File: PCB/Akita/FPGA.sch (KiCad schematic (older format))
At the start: 4 parts

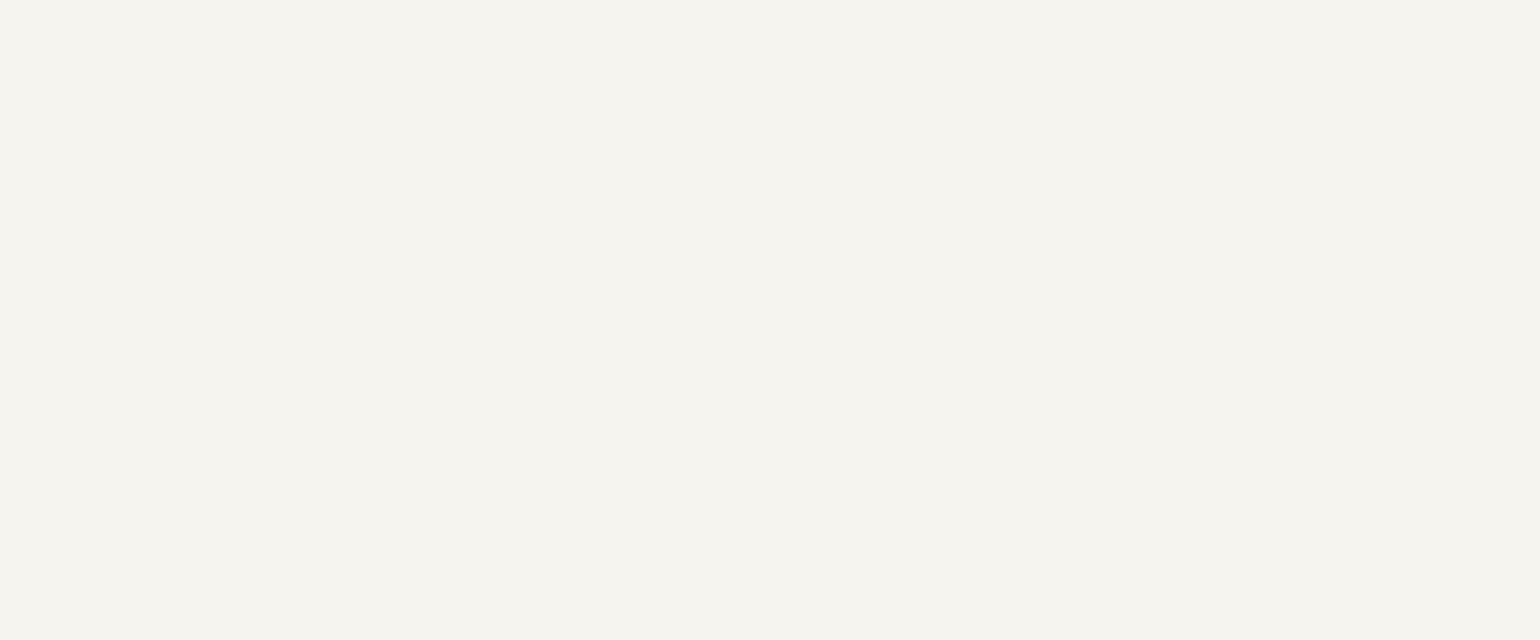
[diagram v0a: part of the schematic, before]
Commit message: Symbols and Power Schematic
Power for FPGA schematic laid out, schematic symbols for resistors and caps replaced with standard ones.
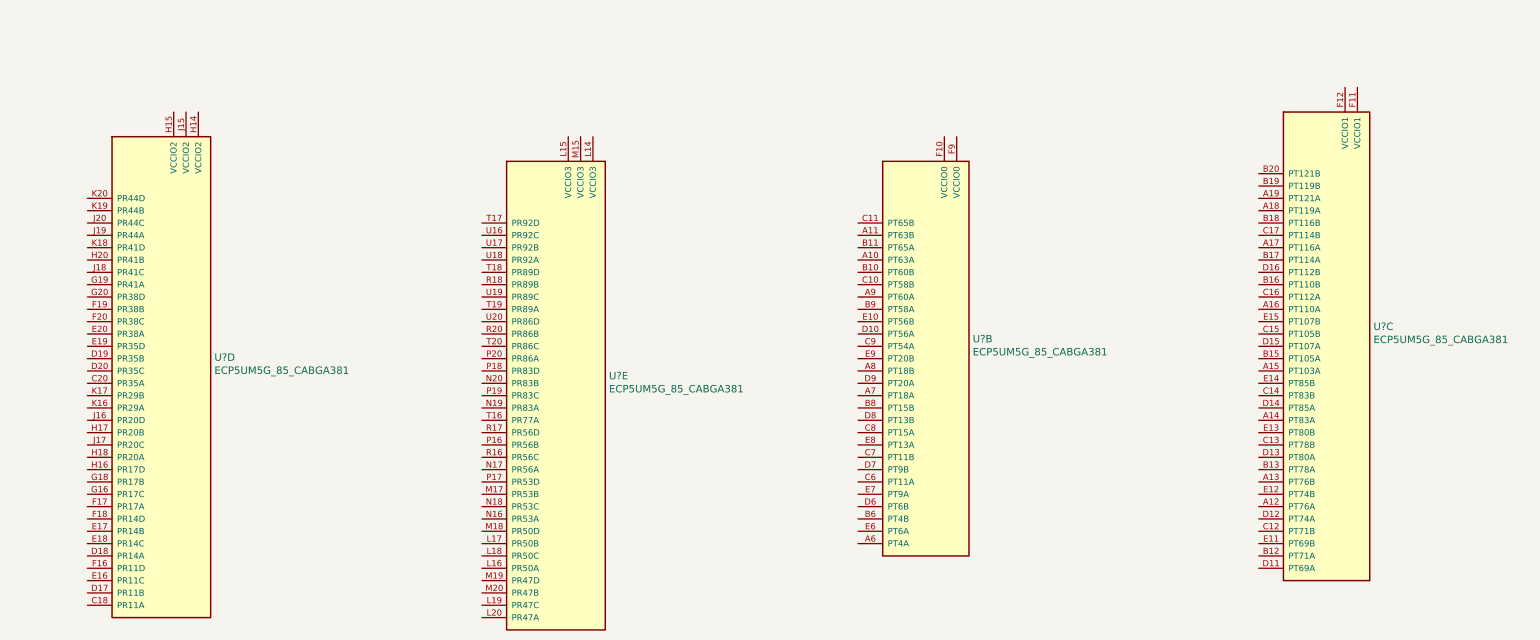
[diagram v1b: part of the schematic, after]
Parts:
- added U? (x4): ECP5UM5G_85_CABGA381, symbol Akita_Pro_Library:ECP5UM5G_85_CABGA381
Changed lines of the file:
@@
 EELAYER 29 0
 EELAYER END
-$Descr A4 11693 8268
+$Descr A2 23386 16535
 encoding utf-8
 Sheet 3 7
@@
 	1    0    0    -1
 $EndComp
+$Comp
+L Akita_Pro_Library:ECP5UM5G_85_CABGA381 U?
+U 4 1 5CEC630A
+P 9250 2850
+F 0 "U?" H 10280 1560 60  0000 L CNN
+F 1 "ECP5UM5G_85_CABGA381" H 10280 1454 60  0000 L CNN
+F 2 "" H 9250 2850 50  0001 C CNN
+F 3 "" H 9250 2850 50  0001 C CNN
+F 4 "ECP5UM5G_85" H 9400 2800 60  0001 R CNN "manf#"
+	4    9250 2850
+	1    0    0    -1
+$EndComp
+$Comp
+L Akita_Pro_Library:ECP5UM5G_85_CABGA381 U?
+U 5 1 5CECF03B
+P 12450 3050
+F 0 "U?" H 13480 1810 60  0000 L CNN
+F 1 "ECP5UM5G_85_CABGA381" H 13480 1704 60  0000 L CNN
+F 2 "" H 12450 3050 50  0001 C CNN
+F 3 "" H 12450 3050 50  0001 C CNN
+F 4 "ECP5UM5G_85" H 12600 3000 60  0001 R CNN "manf#"
+	5    12450 3050
+	1    0    0    -1
+$EndComp
+$Comp
+L Akita_Pro_Library:ECP5UM5G_85_CABGA381 U?
+U 2 1 5CED7F29
+P 15500 3050
+F 0 "U?" H 16430 2110 60  0000 L CNN
+F 1 "ECP5UM5G_85_CABGA381" H 16430 2004 60  0000 L CNN
+F 2 "" H 15500 3050 50  0001 C CNN
+F 3 "" H 15500 3050 50  0001 C CNN
+F 4 "ECP5UM5G_85" H 15650 3000 60  0001 R CNN "manf#"
+	2    15500 3050
+	1    0    0    -1
+$EndComp
+$Comp
+L Akita_Pro_Library:ECP5UM5G_85_CABGA381 U?
+U 3 1 5CEE12E2
+P 18750 2650
+F 0 "U?" H 19680 1410 60  0000 L CNN
+F 1 "ECP5UM5G_85_CABGA381" H 19680 1304 60  0000 L CNN
+F 2 "" H 18750 2650 50  0001 C CNN
+F 3 "" H 18750 2650 50  0001 C CNN
+F 4 "ECP5UM5G_85" H 18900 2600 60  0001 R CNN "manf#"
+	3    18750 2650
+	1    0    0    -1
+$EndComp
